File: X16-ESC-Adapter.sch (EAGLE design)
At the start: 4 parts, among them J1 CONN_1824750000

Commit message: Curren tprogress on schem
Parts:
- removed J1: CONN_1824750000, X16-ESC-Adapter:CONN_1824750000
- removed U$1: CONN_BACKPLANE_ESC_ADAPTER, X16-ESC-Adapter:CONN_BACKPLANE_ESC_ADAPTER
- removed U$2: CONN_JST_8_PIN, X16-ESC-Adapter:CONN_JST_8_PIN
- removed U$3: LUMENIER, X16-ESC-Adapter:LUMENIER
- added D1: GREEN, SparkFun-LED:LED0603
- added ESC1, ESC2, ESC3, ESC4: CONN_1824750000, X16-ESC-Adapter:CONN_1824750000
- added LUMENIER_ESC_PORT: CONN_JST_8_PIN, X16-ESC-Adapter:CONN_JST_8_PIN
- added LUMINIER_ESC: LUMENIER, X16-ESC-Adapter:LUMENIER
- added PWR: CONN_BACKPLANE_ESC_ADAPTER, X16-ESC-Adapter:CONN_BACKPLANE_ESC_ADAPTER
- added RIZZ: 600, SparkFun-Resistors:0.1OHM-0603-1/3W-1%
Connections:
- new net 12V: LUMINIER_ESC.VIN, PWR.12V, RIZZ.1
- new net ESC1A: ESC1.1, ESC1.2, LUMINIER_ESC.M1P1
- new net ESC1B: ESC1.3, ESC1.4, LUMINIER_ESC.M1P2
- new net ESC1C: ESC1.5, ESC1.6, LUMINIER_ESC.M1P3
- new net ESC2A: ESC2.1, ESC2.2, LUMINIER_ESC.M2P1
- new net ESC2B: ESC2.3, ESC2.4, LUMINIER_ESC.M2P2
- new net ESC2C: ESC2.5, ESC2.6, LUMINIER_ESC.M2P3
- new net ESC3A: ESC3.5, ESC3.6, LUMINIER_ESC.M4P1
- new net ESC3B: ESC3.3, ESC3.4, LUMINIER_ESC.M4P2
- new net ESC3C: ESC3.1, ESC3.2, LUMINIER_ESC.M4P3
- new net ESC4A: ESC4.5, ESC4.6, LUMINIER_ESC.M3P1
- new net ESC4B: ESC4.3, ESC4.4, LUMINIER_ESC.M3P2
- new net ESC4C: ESC4.1, ESC4.2, LUMINIER_ESC.M3P3
- new net GND: D1.C, LUMENIER_ESC_PORT.LIPO_GND, LUMINIER_ESC.GND, PWR.GND
- new net MTR_1: LUMENIER_ESC_PORT.MTR_1, PWR.PWM0
- new net MTR_2: LUMENIER_ESC_PORT.MTR_2, PWR.PWM1
- new net MTR_3: LUMENIER_ESC_PORT.MTR_3, PWR.PWM2
- new net MTR_4: LUMENIER_ESC_PORT.MTR_4, PWR.PWM3
- new net N$1: D1.A, RIZZ.2
- new net N$7: PWR.NC

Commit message: Finished Layout
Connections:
- removed net N$7: PWR.NC
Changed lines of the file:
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@@
 <grid distance="0.1" unitdist="inch" unit="inch" style="lines" multiple="1" display="no" altdistance="0.01" altunitdist="inch" altunit="inch"/>
 <layers>
-<layer number="1" name="Top" color="4" fill="1" visible="yes" active="no"/>
-<layer number="16" name="Bottom" color="1" fill="1" visible="yes" active="no"/>
-<layer number="17" name="Pads" color="2" fill="1" visible="yes" active="no"/>
-<layer number="18" name="Vias" color="2" fill="1" visible="yes" active="no"/>
-<layer number="19" name="Unrouted" color="6" fill="1" visible="yes" active="no"/>
-<layer number="20" name="Dimension" color="24" fill="1" visible="yes" active="no"/>
-<layer number="21" name="tPlace" color="7" fill="1" visible="yes" active="no"/>
-<layer number="22" name="bPlace" color="7" fill="1" visible="yes" active="no"/>
-<layer number="23" name="tOrigins" color="15" fill="1" visible="yes" active="no"/>
-<layer number="24" name="bOrigins" color="15" fill="1" visible="yes" active="no"/>
-<layer number="25" name="tNames" color="7" fill="1" visible="yes" active="no"/>
-<layer number="26" name="bNames" color="7" fill="1" visible="yes" active="no"/>
-<layer number="27" name="tValues" color="7" fill="1" visible="yes" active="no"/>
-<layer number="28" name="bValues" color="7" fill="1" visible="yes" active="no"/>
+<layer number="1" name="Top" color="4" fill="1" visible="no" active="no"/>
+<layer number="16" name="Bottom" color="1" fill="1" visible="no" active="no"/>
+<layer number="17" name="Pads" color="2" fill="1" visible="no" active="no"/>
+<layer number="18" name="Vias" color="2" fill="1" visible="no" active="no"/>
+<layer number="19" name="Unrouted" color="6" fill="1" visible="no" active="no"/>
+<layer number="20" name="Dimension" color="24" fill="1" visible="no" active="no"/>
+<layer number="21" name="tPlace" color="7" fill="1" visible="no" active="no"/>
+<layer number="22" name="bPlace" color="7" fill="1" visible="no" active="no"/>
+<layer number="23" name="tOrigins" color="15" fill="1" visible="no" active="no"/>
+<layer number="24" name="bOrigins" color="15" fill="1" visible="no" active="no"/>
+<layer number="25" name="tNames" color="7" fill="1" visible="no" active="no"/>
+<layer number="26" name="bNames" color="7" fill="1" visible="no" active="no"/>
+<layer number="27" name="tValues" color="7" fill="1" visible="no" active="no"/>
+<layer number="28" name="bValues" color="7" fill="1" visible="no" active="no"/>
 <layer number="29" name="tStop" color="7" fill="3" visible="no" active="no"/>
 <layer number="30" name="bStop" color="7" fill="6" visible="no" active="no"/>
@@
 <layer number="35" name="tGlue" color="7" fill="4" visible="no" active="no"/>
 <layer number="36" name="bGlue" color="7" fill="5" visible="no" active="no"/>
-<layer number="37" name="tTest" color="7" fill="1" visible="yes" active="no"/>
-<layer number="38" name="bTest" color="7" fill="1" visible="yes" active="no"/>
+<layer number="37" name="tTest" color="7" fill="1" visible="no" active="no"/>
+<layer number="38" name="bTest" color="7" fill="1" visible="no" active="no"/>
 <layer number="39" name="tKeepout" color="4" fill="11" visible="no" active="no"/>
 <layer number="40" name="bKeepout" color="1" fill="11" visible="no" active="no"/>
@@
 <layer number="44" name="Drills" color="7" fill="1" visible="no" active="no"/>
 <layer number="45" name="Holes" color="7" fill="1" visible="no" active="no"/>
-<layer number="46" name="Milling" color="3" fill="1" visible="yes" active="no"/>
-<layer number="47" name="Measures" color="7" fill="1" visible="yes" active="no"/>
-<layer number="48" name="Document" color="7" fill="1" visible="yes" active="no"/>
-<layer number="49" name="Reference" color="7" fill="1" visible="yes" active="no"/>
-<layer number="50" name="dxf" color="7" fill="1" visible="yes" active="no"/>
-<layer number="51" name="tDocu" color="7" fill="1" visible="yes" active="no"/>
-<layer number="52" name="bDocu" color="7" fill="1" visible="yes" active="no"/>
-<layer number="53" name="tGND_GNDA" color="7" fill="9" visible="yes" active="no"/>
-<layer number="54" name="bGND_GNDA" color="1" fill="9" visible="yes" active="no"/>
-<layer number="56" name="wert" color="7" fill="1" visible="yes" active="no"/>
-<layer number="57" name="tCAD" color="7" fill="1" visible="yes" active="no"/>
-<layer number="58" name="bCAD" color="7" fill="1" visible="yes" active="no"/>
-<layer number="59" name="tCarbon" color="7" fill="1" visible="yes" active="no"/>
-<layer number="60" name="bCarbon" color="7" fill="1" visible="yes" active="no"/>
+<layer number="46" name="Milling" color="3" fill="1" visible="no" active="no"/>
+<layer number="47" name="Measures" color="7" fill="1" visible="no" active="no"/>
+<layer number="48" name="Document" color="7" fill="1" visible="no" active="no"/>
+<layer number="49" name="Reference" color="7" fill="1" visible="no" active="no"/>
+<layer number="50" name="dxf" color="7" fill="1" visible="no" active="no"/>
+<layer number="51" name="tDocu" color="7" fill="1" visible="no" active="no"/>
+<layer number="52" name="bDocu" color="7" fill="1" visible="no" active="no"/>
+<layer number="53" name="tGND_GNDA" color="7" fill="9" visible="no" active="no"/>
+<layer number="54" name="bGND_GNDA" color="1" fill="9" visible="no" active="no"/>
+<layer number="56" name="wert" color="7" fill="1" visible="no" active="no"/>
+<layer number="57" name="tCAD" color="7" fill="1" visible="no" active="no"/>
+<layer number="58" name="bCAD" color="7" fill="1" visible="no" active="no"/>
+<layer number="59" name="tCarbon" color="7" fill="1" visible="no" active="no"/>
+<layer number="60" name="bCarbon" color="7" fill="1" visible="no" active="no"/>
 <layer number="88" name="SimResults" color="9" fill="1" visible="yes" active="yes"/>
 <layer number="89" name="SimProbes" color="9" fill="1" visible="yes" active="yes"/>
@@
 </segment>
 </net>
-<net name="N$7" class="0">
-<segment>
-<pinref part="PWR" gate="G$1" pin="NC"/>
-<wire x1="50.8" y1="-33.02" x2="53.34" y2="-33.02" width="0.1524" layer="91"/>
-</segment>
-</net>

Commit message: Update X16-ESC-Adapter.sch
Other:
- note added: "Connectors to Thrusters"
- note added: "ESC"
- note added: "ESC Port"
- note added: "Power In/Out"
- note added: "Power Tester Light"
- moved on the sheet: D1, ESC1, ESC2, ESC3, ESC4, LUMENIER_ESC_PORT, LUMINIER_ESC, PWR, RIZZ

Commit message: First set of changes after alumni design review
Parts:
- removed D1: GREEN, SparkFun-LED:LED0603
- added HOPE: (no value), led:LEDCHIPLED_0805
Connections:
- net GND: now also HOPE.C; no longer D1.C
- net N$1: now also HOPE.A; no longer D1.A
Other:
- moved on the sheet: ESC1, ESC2, ESC3, ESC4, LUMENIER_ESC_PORT, LUMINIER_ESC, PWR, RIZZ

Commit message: Updated (11/4)
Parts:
- removed LUMENIER_ESC_PORT: CONN_JST_8_PIN, X16-ESC-Adapter:CONN_JST_8_PIN
- added J1: BM08B-SRSS-TB(LF)(SN), X16-ESC-Adapter:BM08B-SRSS-TB(LF)(SN)
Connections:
- net GND: now also J1.SHIELD; no longer LUMENIER_ESC_PORT.LIPO_GND
- net MTR_1: now also J1.1; no longer LUMENIER_ESC_PORT.MTR_1
- net MTR_2: now also J1.2; no longer LUMENIER_ESC_PORT.MTR_2
- net MTR_3: now also J1.3; no longer LUMENIER_ESC_PORT.MTR_3
- net MTR_4: now also J1.4; no longer LUMENIER_ESC_PORT.MTR_4
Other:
- moved on the sheet: ESC1, ESC2, ESC3, ESC4, HOPE, LUMINIER_ESC, PWR, RIZZ

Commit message: Finished!
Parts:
- PWR: device X16-ESC-Adapter:CONN_BACKPLANE_ESC_ADAPTER -> X16-NewESCAdapterConn:CONN_BACKPLANE_ESC_ADAPTER
- renumbered RIZZ to 600
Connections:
- net GND: now also J1.2, PWR.NC; no longer J1.SHIELD
- net MTR_1: now also J1.5; no longer J1.1
- net MTR_2: now also J1.6; no longer J1.2
- net MTR_3: now also J1.7; no longer J1.3
- net MTR_4: now also J1.8; no longer J1.4
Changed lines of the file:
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@@
 <part name="FRAME1" library="SparkFun-Aesthetics" library_urn="urn:adsk.eagle:library:507" deviceset="FRAME-A4L" device=""/>
 <part name="ESC1" library="X16-ESC-Adapter" deviceset="CONN_1824750000" device=""/>
-<part name="PWR" library="X16-ESC-Adapter" deviceset="CONN_BACKPLANE_ESC_ADAPTER" device=""/>
+<part name="PWR" library="X16-NewESCAdapterConn" deviceset="CONN_BACKPLANE_ESC_ADAPTER" device=""/>
 <part name="LUMINIER_ESC" library="X16-ESC-Adapter" deviceset="LUMENIER" device="" package3d_urn="urn:adsk.eagle:package:37886188/1"/>
 <part name="ESC2" library="X16-ESC-Adapter" deviceset="CONN_1824750000" device=""/>
 <part name="ESC3" library="X16-ESC-Adapter" deviceset="CONN_1824750000" device=""/>
 <part name="ESC4" library="X16-ESC-Adapter" deviceset="CONN_1824750000" device=""/>
-<part name="RIZZ" library="SparkFun-Resistors" library_urn="urn:adsk.eagle:library:532" deviceset="0.1OHM" device="-0603-1/3W-1%" package3d_urn="urn:adsk.eagle:package:41389018/1" value="600"/>
+<part name="600" library="SparkFun-Resistors" library_urn="urn:adsk.eagle:library:532" deviceset="0.1OHM" device="-0603-1/3W-1%" package3d_urn="urn:adsk.eagle:package:41389018/1" value="600"/>
 <part name="HOPE" library="led" library_urn="urn:adsk.eagle:library:259" deviceset="LED" device="CHIPLED_0805" package3d_urn="urn:adsk.eagle:package:15821/2"/>
 <part name="J1" library="X16-ESC-Adapter" deviceset="BM08B-SRSS-TB(LF)(SN)" device=""/>
@@
 <attribute name="NAME" x="-39.7256" y="9.9314" size="2.0828" layer="95" ratio="6" rot="SR180"/>
 </instance>
-<instance part="RIZZ" gate="G$1" x="-55.88" y="53.34" smashed="yes">
+<instance part="600" gate="G$1" x="-55.88" y="53.34" smashed="yes">
 <attribute name="NAME" x="-55.88" y="54.864" size="1.778" layer="95" font="vector" align="bottom-center"/>
 <attribute name="VALUE" x="-55.88" y="51.816" size="1.778" layer="96" font="vector" align="top-center"/>
@@
 </segment>
 <segment>
-<pinref part="RIZZ" gate="G$1" pin="1"/>
+<pinref part="600" gate="G$1" pin="1"/>
 <wire x1="-60.96" y1="53.34" x2="-63.5" y2="53.34" width="0.1524" layer="91"/>
 <label x="-63.5" y="53.34" size="1.778" layer="95" rot="R180" xref="yes"/>
@@
 </segment>
 <segment>
-<pinref part="J1" gate="G$1" pin="SHIELD"/>
-<wire x1="-40.64" y1="-33.02" x2="-38.1" y2="-33.02" width="0.1524" layer="91"/>
-<label x="-38.1" y="-33.02" size="1.778" layer="95" xref="yes"/>
+<pinref part="PWR" gate="G$1" pin="NC"/>
+<wire x1="45.72" y1="-30.48" x2="48.26" y2="-30.48" width="0.1524" layer="91"/>
+<label x="48.26" y="-30.48" size="1.778" layer="95" xref="yes"/>
+</segment>
+<segment>
+<pinref part="J1" gate="G$1" pin="2"/>
+<wire x1="-40.64" y1="-53.34" x2="-38.1" y2="-53.34" width="0.1524" layer="91"/>
+<label x="-38.1" y="-53.34" size="1.778" layer="95" xref="yes"/>
 </segment>
 </net>
@@
 </segment>
 <segment>
-<pinref part="J1" gate="G$1" pin="1"/>
-<wire x1="-40.64" y1="-55.88" x2="-38.1" y2="-55.88" width="0.1524" layer="91"/>
-<label x="-38.1" y="-55.88" size="1.778" layer="95" xref="yes"/>
+<pinref part="J1" gate="G$1" pin="5"/>
+<wire x1="-40.64" y1="-45.72" x2="-38.1" y2="-45.72" width="0.1524" layer="91"/>
+<label x="-38.1" y="-45.72" size="1.778" layer="95" xref="yes"/>
 </segment>
 </net>
@@
 </segment>
 <segment>
-<pinref part="J1" gate="G$1" pin="2"/>
-<wire x1="-40.64" y1="-53.34" x2="-38.1" y2="-53.34" width="0.1524" layer="91"/>
-<label x="-38.1" y="-53.34" size="1.778" layer="95" xref="yes"/>
+<pinref part="J1" gate="G$1" pin="6"/>
+<wire x1="-40.64" y1="-43.18" x2="-38.1" y2="-43.18" width="0.1524" layer="91"/>
+<label x="-38.1" y="-43.18" size="1.778" layer="95" xref="yes"/>
 </segment>
 </net>
@@
 </segment>
 <segment>
-<pinref part="J1" gate="G$1" pin="3"/>
-<wire x1="-40.64" y1="-50.8" x2="-38.1" y2="-50.8" width="0.1524" layer="91"/>
-<label x="-38.1" y="-50.8" size="1.778" layer="95" xref="yes"/>
+<pinref part="J1" gate="G$1" pin="7"/>
+<wire x1="-40.64" y1="-40.64" x2="-38.1" y2="-40.64" width="0.1524" layer="91"/>
+<label x="-38.1" y="-40.64" size="1.778" layer="95" xref="yes"/>
 </segment>
 </net>
@@
 </segment>
 <segment>
-<pinref part="J1" gate="G$1" pin="4"/>
-<wire x1="-40.64" y1="-48.26" x2="-38.1" y2="-48.26" width="0.1524" layer="91"/>
-<label x="-38.1" y="-48.26" size="1.778" layer="95" xref="yes"/>
+<pinref part="J1" gate="G$1" pin="8"/>
+<wire x1="-40.64" y1="-38.1" x2="-38.1" y2="-38.1" width="0.1524" layer="91"/>
+<label x="-38.1" y="-38.1" size="1.778" layer="95" xref="yes"/>
 </segment>
 </net>
 <net name="N$1" class="0">
 <segment>
-<pinref part="RIZZ" gate="G$1" pin="2"/>
+<pinref part="600" gate="G$1" pin="2"/>
 <wire x1="-50.8" y1="53.34" x2="-48.26" y2="53.34" width="0.1524" layer="91"/>
 <pinref part="HOPE" gate="G$1" pin="A"/>

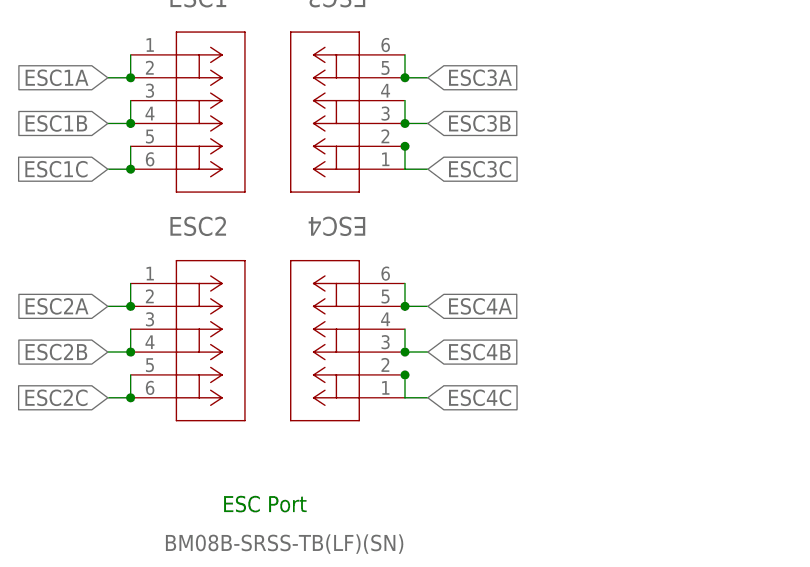
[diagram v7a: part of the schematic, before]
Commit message: added junctions + moved LED to left
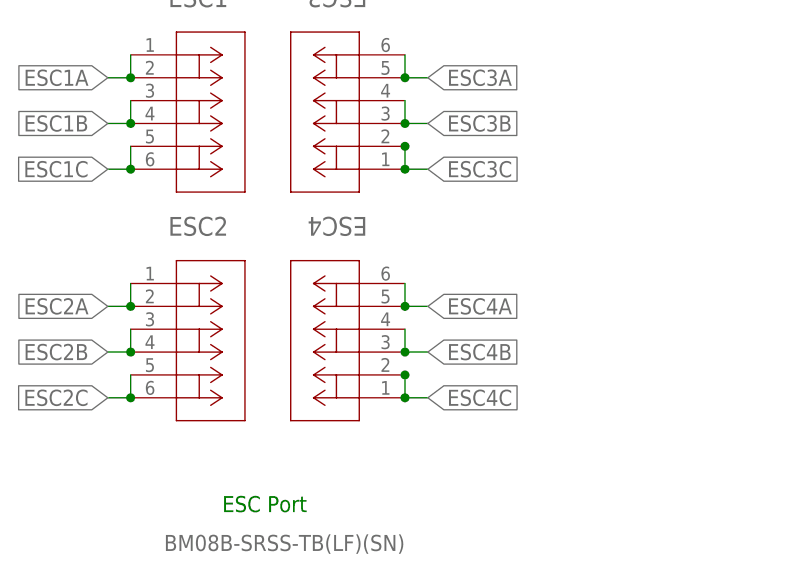
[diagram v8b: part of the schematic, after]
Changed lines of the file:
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@@
 <junction x="-35.56" y="17.78"/>
 <label x="-33.02" y="15.24" size="1.778" layer="95" xref="yes"/>
+<junction x="-35.56" y="15.24"/>
 </segment>
 <segment>
@@
 <junction x="-35.56" y="-7.62"/>
 <label x="-33.02" y="-10.16" size="1.778" layer="95" xref="yes"/>
+<junction x="-35.56" y="-10.16"/>
 </segment>
 <segment>
